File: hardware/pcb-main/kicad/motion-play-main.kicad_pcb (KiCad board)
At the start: 4 copper layers, 101.4 x 40 mm, 86 parts, among them IC1 SN74AHCT125PWR, J3 LED_Strip, J4 Conn_01x05, J5 Conn_01x05, J6 Conn_01x05, J7 TYPE-C-31-M-12, J8 JST_PH_2pin, Q2 PMOS, U1 AP2112K-3.3TRG1, U2 T-Display-S3, U4 TCA9548APWR, U5 BQ24195RGER, U6 TPS61088RHLR, U7 INA219AIDCNR

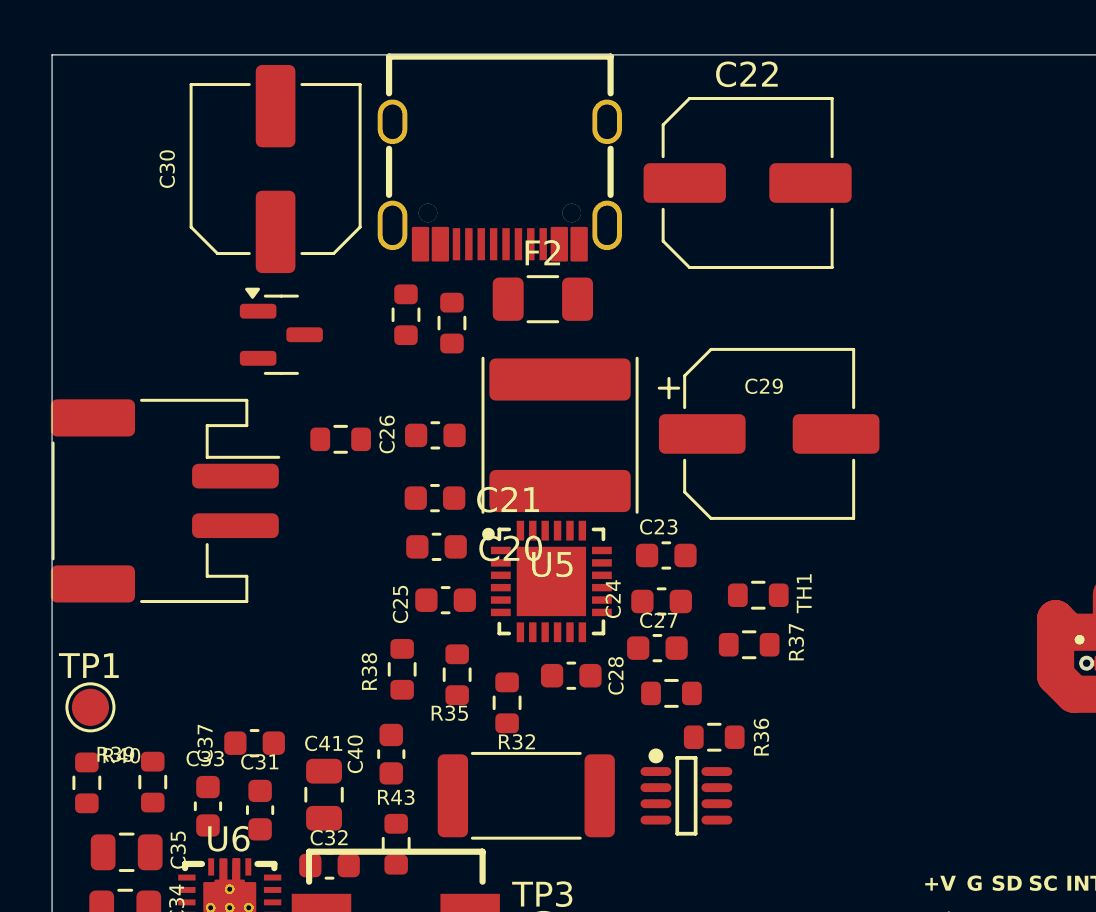
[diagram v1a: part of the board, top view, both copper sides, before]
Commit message: Phase 3 complete: shift L1 up 2mm, re-place C23 to 3mm from BTST, run DRC
L1 moved from y=116.35 to y=114.35, opening a 2.1mm gap between L1 and U5.
C23 BTST bridging cap improved from 4.5mm (relaxed) to 3.0mm (within Tier 1).
Relaxation count reduced from 4 to 2 (only L2 and C41 remain relaxed).

DRC: 84 violations total — 56 from J7/U6 footprint imports (pre-existing),
17 silkscreen overlaps (cosmetic), 9 dangling tracks (pre-existing),
2 R42 edge clearance (only placement-caused issue). 137 unconnected items
expected pre-routing. No component overlap violations.

Made-with: Cursor
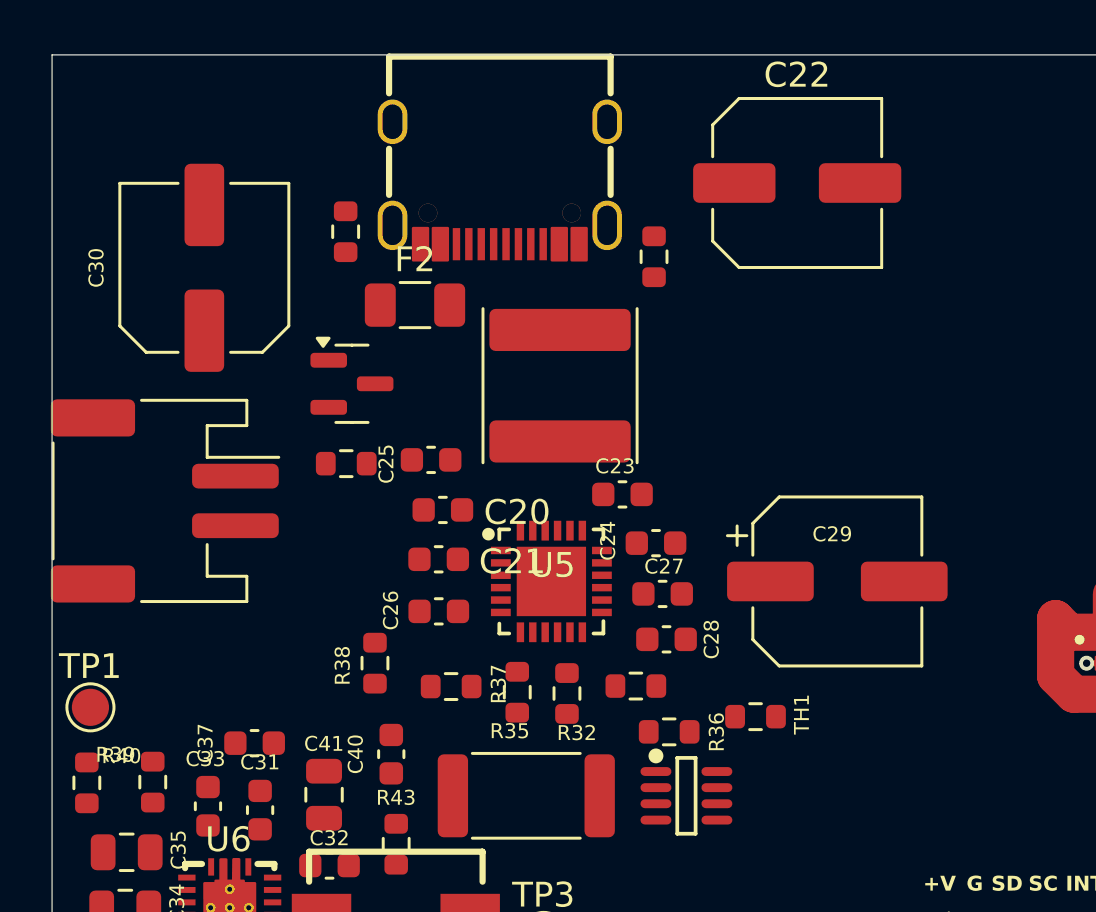
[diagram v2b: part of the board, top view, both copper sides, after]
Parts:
- moved R37 12.1 mm to (78.7, 126.5)
- moved R30 8.58 mm to (86.9, 109.1)
- moved C26 7.10 mm to (78.2, 123.5)
- moved C29 6.56 mm to (94.3, 122.2)
- moved C25 5.69 mm to (77.9, 117.3)
- moved F2 5.17 mm to (77.2, 111.1)
- moved C30 4.92 mm to (68.7, 109.6)
- moved TH1 4.90 mm to (91.0, 127.7)
- moved R31 4.14 mm to (74.4, 108.1)
- moved C28 4.11 mm to (87.4, 124.6)
- moved Q2 3.47 mm to (74.7, 114.3)
- moved C23 3.03 mm to (85.6, 118.7)
- moved R35 2.53 mm to (81.4, 126.7)
- moved C21 2.47 mm to (78.2, 121.4)
- moved R32 2.45 mm to (83.4, 126.8)
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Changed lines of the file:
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@@
 	(footprint "Capacitor_SMD:C_0603_1608Metric"
 		(layer "F.Cu")
-		(at 78.067 116.355 180)
+		(at 78.206 123.457 180)
 		(descr "Capacitor SMD 0603 (1608 Metric), square (rectangular) end terminal, IPC-7351 nominal, (Body size source: IPC-SM-782 page 76, https://www.pcb-3d.com/wordpress/wp-content/uploads/ipc-sm-782a_amendment_1_and_2.pdf), generated with kicad-footprint-generator")
 		(tags "capacitor")
@@
 	(footprint "Resistor_SMD:R_0603_1608Metric"
 		(layer "F.Cu")
-		(at 90.732 124.805)
+		(at 78.705 126.491)
 		(descr "Resistor SMD 0603 (1608 Metric), square (rectangular) end terminal, IPC-7351 nominal, (Body size source: IPC-SM-782 page 72, https://www.pcb-3d.com/wordpress/wp-content/uploads/ipc-sm-782a_amendment_1_and_2.pdf), generated with kicad-footprint-generator")
 		(tags "resistor")
@@
 	(footprint "Resistor_SMD:R_0603_1608Metric"
 		(layer "F.Cu")
-		(at 78.948 126.013 -90)
+		(at 81.373 126.72 -90)
 		(descr "Resistor SMD 0603 (1608 Metric), square (rectangular) end terminal, IPC-7351 nominal, (Body size source: IPC-SM-782 page 72, https://www.pcb-3d.com/wordpress/wp-content/uploads/ipc-sm-782a_amendment_1_and_2.pdf), generated with kicad-footprint-generator")
 		(tags "resistor")
@@
 	(footprint "Resistor_SMD:R_0603_1608Metric"
 		(layer "F.Cu")
-		(at 74.247 116.514)
+		(at 74.472 117.496)
 		(descr "Resistor SMD 0603 (1608 Metric), square (rectangular) end terminal, IPC-7351 nominal, (Body size source: IPC-SM-782 page 72, https://www.pcb-3d.com/wordpress/wp-content/uploads/ipc-sm-782a_amendment_1_and_2.pdf), generated with kicad-footprint-generator")
 		(tags "resistor")
@@
 	(footprint "Capacitor_SMD:C_0603_1608Metric"
 		(layer "F.Cu")
-		(at 87.029 124.94)
+		(at 87.239 122.753)
 		(descr "Capacitor SMD 0603 (1608 Metric), square (rectangular) end terminal, IPC-7351 nominal, (Body size source: IPC-SM-782 page 76, https://www.pcb-3d.com/wordpress/wp-content/uploads/ipc-sm-782a_amendment_1_and_2.pdf), generated with kicad-footprint-generator")
 		(tags "capacitor")
@@
 	(footprint "Capacitor_SMD:CP_Elec_6.3x7.7"
 		(layer "F.Cu")
-		(at 91.539 116.296)
+		(at 94.29 122.25)
 		(descr "SMD capacitor, aluminum electrolytic, Nichicon, 6.3x7.7mm")
 		(tags "capacitor electrolytic")
@@
 	(footprint "Package_TO_SOT_SMD:SOT-23"
 		(layer "F.Cu")
-		(at 71.854 112.294)
+		(at 74.702 114.273)
 		(descr "SOT, 3 Pin (JEDEC TO-236 Var AB https://www.jedec.org/document_search?search_api_views_fulltext=TO-236), generated with kicad-footprint-generator ipc_gullwing_generator.py")
 		(tags "SOT TO_SOT_SMD")
@@
 	(footprint "Resistor_SMD:R_0603_1608Metric"
 		(layer "F.Cu")
-		(at 91.1 122.806)
+		(at 90.989 127.706)
 		(descr "Resistor SMD 0603 (1608 Metric), square (rectangular) end terminal, IPC-7351 nominal, (Body size source: IPC-SM-782 page 72, https://www.pcb-3d.com/wordpress/wp-content/uploads/ipc-sm-782a_amendment_1_and_2.pdf), generated with kicad-footprint-generator")
 		(tags "resistor")
@@
 	(footprint "Capacitor_SMD:C_0603_1608Metric"
 		(layer "F.Cu")
-		(at 78.053 118.887)
+		(at 78.202 121.356)
 		(descr "Capacitor SMD 0603 (1608 Metric), square (rectangular) end terminal, IPC-7351 nominal, (Body size source: IPC-SM-782 page 76, https://www.pcb-3d.com/wordpress/wp-content/uploads/ipc-sm-782a_amendment_1_and_2.pdf), generated with kicad-footprint-generator")
 		(tags "capacitor")
@@
 	(footprint "Capacitor_SMD:C_0603_1608Metric"
 		(layer "F.Cu")
-		(at 83.554 126.054)
+		(at 87.397 124.586)
 		(descr "Capacitor SMD 0603 (1608 Metric), square (rectangular) end terminal, IPC-7351 nominal, (Body size source: IPC-SM-782 page 76, https://www.pcb-3d.com/wordpress/wp-content/uploads/ipc-sm-782a_amendment_1_and_2.pdf), generated with kicad-footprint-generator")
 		(tags "capacitor")
@@
 	(footprint "Capacitor_SMD:C_0603_1608Metric"
 		(layer "F.Cu")
-		(at 87.199 123.058 180)
+		(at 86.972 120.704 180)
 		(descr "Capacitor SMD 0603 (1608 Metric), square (rectangular) end terminal, IPC-7351 nominal, (Body size source: IPC-SM-782 page 76, https://www.pcb-3d.com/wordpress/wp-content/uploads/ipc-sm-782a_amendment_1_and_2.pdf), generated with kicad-footprint-generator")
 		(tags "capacitor")
@@
 	(footprint "Capacitor_SMD:C_0603_1608Metric"
 		(layer "F.Cu")
-		(at 78.116 120.854)
+		(at 78.371 119.364)
 		(descr "Capacitor SMD 0603 (1608 Metric), square (rectangular) end terminal, IPC-7351 nominal, (Body size source: IPC-SM-782 page 76, https://www.pcb-3d.com/wordpress/wp-content/uploads/ipc-sm-782a_amendment_1_and_2.pdf), generated with kicad-footprint-generator")
 		(tags "capacitor")
@@
 	(footprint "Resistor_SMD:R_0603_1608Metric"
 		(layer "F.Cu")
-		(at 87.596 126.768)
+		(at 86.159 126.471)
 		(descr "Resistor SMD 0603 (1608 Metric), square (rectangular) end terminal, IPC-7351 nominal, (Body size source: IPC-SM-782 page 72, https://www.pcb-3d.com/wordpress/wp-content/uploads/ipc-sm-782a_amendment_1_and_2.pdf), generated with kicad-footprint-generator")
 		(tags "resistor")
@@
 	(footprint "Capacitor_SMD:C_0603_1608Metric"
 		(layer "F.Cu")
-		(at 78.482 123.006 180)
+		(at 77.896 117.344 180)
 		(descr "Capacitor SMD 0603 (1608 Metric), square (rectangular) end terminal, IPC-7351 nominal, (Body size source: IPC-SM-782 page 76, https://www.pcb-3d.com/wordpress/wp-content/uploads/ipc-sm-782a_amendment_1_and_2.pdf), generated with kicad-footprint-generator")
 		(tags "capacitor")
@@
 	(footprint "Fuse:Fuse_1206_3216Metric"
 		(layer "F.Cu")
-		(at 82.407 110.859)
+		(at 77.246 111.097)
 		(descr "Fuse SMD 1206 (3216 Metric), square (rectangular) end terminal, IPC-7351 nominal, (Body size source: http://www.tortai-tech.com/upload/download/2011102023233369053.pdf), generated with kicad-footprint-generator")
 		(tags "fuse")
@@
 	(footprint "Resistor_SMD:R_0603_1608Metric"
 		(layer "F.Cu")
-		(at 89.323 128.536)
+		(at 87.504 128.32)
 		(descr "Resistor SMD 0603 (1608 Metric), square (rectangular) end terminal, IPC-7351 nominal, (Body size source: IPC-SM-782 page 72, https://www.pcb-3d.com/wordpress/wp-content/uploads/ipc-sm-782a_amendment_1_and_2.pdf), generated with kicad-footprint-generator")
 		(tags "resistor")
@@
 	(footprint "Capacitor_SMD:C_0603_1608Metric"
 		(layer "F.Cu")
-		(at 87.387 121.201 180)
+		(at 85.619 118.737 180)
 		(descr "Capacitor SMD 0603 (1608 Metric), square (rectangular) end terminal, IPC-7351 nominal, (Body size source: IPC-SM-782 page 76, https://www.pcb-3d.com/wordpress/wp-content/uploads/ipc-sm-782a_amendment_1_and_2.pdf), generated with kicad-footprint-generator")
 		(tags "capacitor")
@@
 	(footprint "Resistor_SMD:R_0603_1608Metric"
 		(layer "F.Cu")
-		(at 78.738 111.822 -90)
+		(at 86.894 109.146 -90)
 		(descr "Resistor SMD 0603 (1608 Metric), square (rectangular) end terminal, IPC-7351 nominal, (Body size source: IPC-SM-782 page 72, https://www.pcb-3d.com/wordpress/wp-content/uploads/ipc-sm-782a_amendment_1_and_2.pdf), generated with kicad-footprint-generator")
 		(tags "resistor")
@@
 	(footprint "Resistor_SMD:R_0603_1608Metric"
 		(layer "F.Cu")
-		(at 80.963 127.147 -90)
+		(at 83.379 126.771 -90)
 		(descr "Resistor SMD 0603 (1608 Metric), square (rectangular) end terminal, IPC-7351 nominal, (Body size source: IPC-SM-782 page 72, https://www.pcb-3d.com/wordpress/wp-content/uploads/ipc-sm-782a_amendment_1_and_2.pdf), generated with kicad-footprint-generator")
 		(tags "resistor")
@@
 	(footprint "Capacitor_SMD:C_Elec_6.3x5.4"
 		(layer "F.Cu")
-		(at 90.67 106.17)
+		(at 92.67 106.17)
 		(descr "SMD capacitor, aluminum electrolytic nonpolar, 6.3x5.4mm")
 		(tags "capacitor electrolytic nonpolar")
@@
 	(footprint "Resistor_SMD:R_0603_1608Metric"
 		(layer "F.Cu")
-		(at 76.729 125.797 -90)
+		(at 75.631 125.547 -90)
 		(descr "Resistor SMD 0603 (1608 Metric), square (rectangular) end terminal, IPC-7351 nominal, (Body size source: IPC-SM-782 page 72, https://www.pcb-3d.com/wordpress/wp-content/uploads/ipc-sm-782a_amendment_1_and_2.pdf), generated with kicad-footprint-generator")
 		(tags "resistor")
@@
 	(footprint "Inductor_SMD:L_Changjiang_FNR6028S"
 		(layer "F.Cu")
-		(at 83.1 116.35 90)
+		(at 83.1 114.35 90)
 		(descr "Inductor, Changjiang, FNR6028S, 6.0x6.0x2.8mm, (https://datasheet.lcsc.com/lcsc/1806131217_cjiang-Changjiang-Microelectronics-Tech-FNR5040S3R3NT_C167960.pdf), generated with kicad-footprint-generator gen_inductor.py")
 		(tags "wirewound power shielded")
@@
 	(footprint "Resistor_SMD:R_0603_1608Metric"
 		(layer "F.Cu")
-		(at 76.883 111.487 -90)
+		(at 74.448 108.136 -90)
 		(descr "Resistor SMD 0603 (1608 Metric), square (rectangular) end terminal, IPC-7351 nominal, (Body size source: IPC-SM-782 page 72, https://www.pcb-3d.com/wordpress/wp-content/uploads/ipc-sm-782a_amendment_1_and_2.pdf), generated with kicad-footprint-generator")
 		(tags "resistor")
@@
 	(footprint "Capacitor_SMD:C_Elec_6.3x5.4"
 		(layer "F.Cu")
-		(at 71.621 105.606 90)
+		(at 68.745 109.593 90)
 		(descr "SMD capacitor, aluminum electrolytic nonpolar, 6.3x5.4mm")
 		(tags "capacitor electrolytic nonpolar")

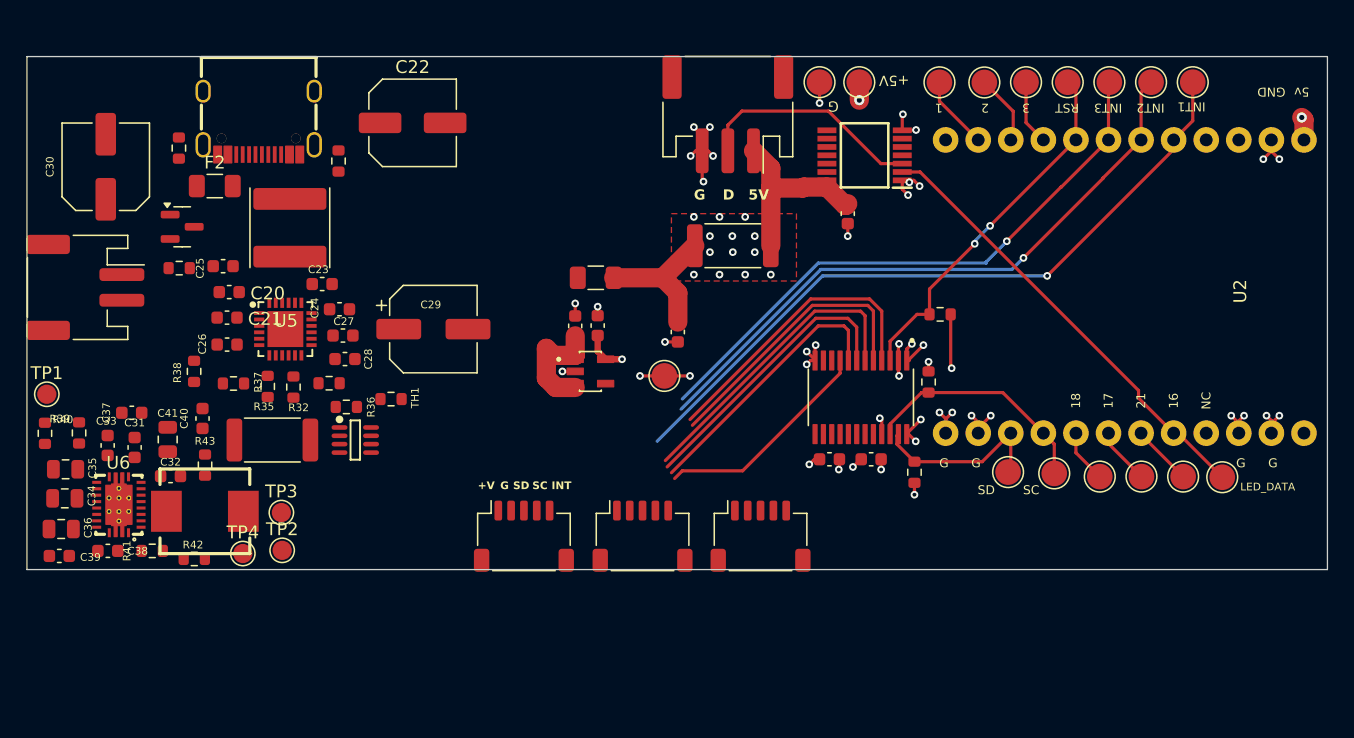
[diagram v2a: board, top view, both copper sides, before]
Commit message: Fix L2 bbox, re-place power components, complete full board routing
- Fix extract.py inductor bbox heuristic: parse L{X}-W{Y} from footprint
  name when pad-based bbox height < width/2 (L2: 8.4×3.2 → 8.4×6.6mm)
- Add L2 to placement anchors, re-run placement pushing C32/R41/R42/R43/TP4
  out of L2's physical footprint
- Fix J7 USB-C schematic pin-to-footprint mapping (A4→A4B9, etc.)
- Complete all trace routing: power switching loops (BOOST_SW pour, BQ_SW),
  VSYS/VBAT/Protected_VBUS power paths, INA219 Kelvin sense, +5V distribution
  via In2.Cu zone, I2C bus, all U5/U6 support passives
- Board setup: net classes, design rules, zone fills
- DRC: 0 unconnected pads, remaining violations are easyeda2kicad footprint
  artifacts (U6 thermal vias, J7 pad spacing) and expected tight QFN escapes

Made-with: Cursor
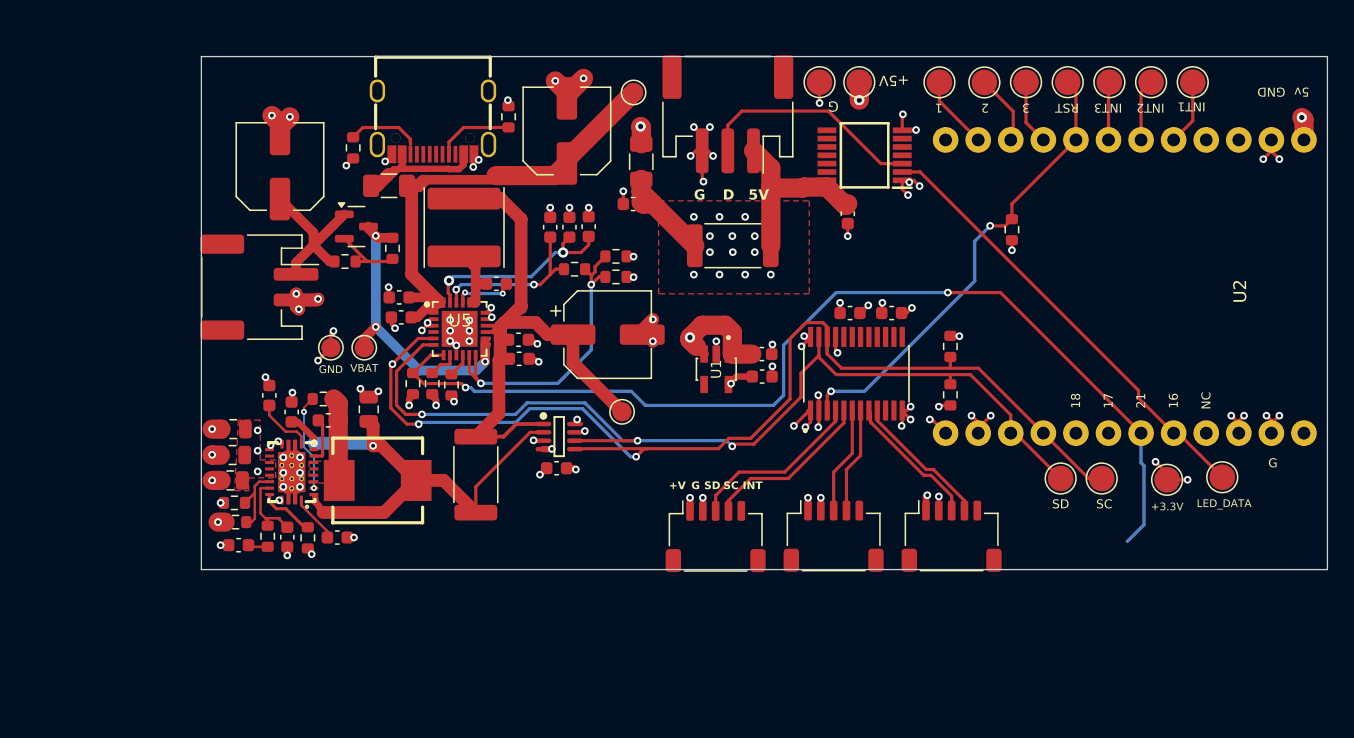
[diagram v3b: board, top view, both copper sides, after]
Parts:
- removed TPIO17, TPIO18, TPIO21: TestPoint, TestPoint:TestPoint_Pad_D2.0mm
- moved TP1 44.9 mm to (109.0, 128.7)
- moved TP3 42.7 mm to (109.9, 103.8)
- moved TP_3V1 40.0 mm to (151.5, 134.0)
- moved J6 33.3 mm to (134.7, 138.4)
- moved R37 31.0 mm to (108.5, 118.2)
- moved C25 28.7 mm to (106.4, 114.3), turned to 90 degrees
- moved C26 28.2 mm to (104.9, 114.3), turned to 90 degrees
- moved C40 27.9 mm to (103.9, 133.1), turned to 180 degrees
- moved R36 20.8 mm to (105.3, 117.6)
- moved TH1 20.8 mm to (108.5, 116.6)
- moved C33 19.3 mm to (86.8, 138.5), turned to 0 degrees
- moved C39 17.8 mm to (82.9, 138.5), turned to -90 degrees
- moved R41 17.8 mm to (85.7, 127.7)
- moved C24 17.6 mm to (103.4, 114.3), turned to 90 degrees
- moved TP4 17.5 mm to (86.3, 123.7)
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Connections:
- J7 pad A1B12: (no net) -> GND
- J7 pad A4B9: (no net) -> /Power Management/VBUS_RAW
- J7 pad B1A12: (no net) -> GND
- J7 pad B4A9: (no net) -> /Power Management/VBUS_RAW
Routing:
- net /Power Management/CHRG_INT: track 4.75 -> 80.4 mm, vias 0 -> 2
- net /I2C_SCL: track 19.4 -> 88.1 mm, vias 0 -> 3
- net /I2C_SDA: track 14.8 -> 76.8 mm, vias 0 -> 3
- net /INT1: track 55.6 -> 5.86 mm, vias 1 -> 0
- net /Power Management/VSYS: track 0.00 -> 47.5 mm
- net /INT2: track 49.6 -> 5.04 mm, vias 1 -> 0
- net GND: track 50.1 -> 94.0 mm, vias 49 -> 113
- net /INT3: track 46.6 -> 4.98 mm, vias 1 -> 0
- net /Power Management/VSYS_SENSE: track 0.00 -> 39.7 mm, vias 0 -> 2
- net /Power Management/Protected_VBUS: track 0.00 -> 35.9 mm
- net /Power Management/BQ_TS: track 0.00 -> 24.4 mm, vias 0 -> 2
- net /Power Management/VBAT: track 0.00 -> 23.2 mm, vias 0 -> 3
- net /Power Management/BQ_PMID: track 0.00 -> 15.9 mm, vias 0 -> 2
- net /TCA9548A_Subsystem/CH1_SDA: track 24.0 -> 8.40 mm
- net /Power Management/VBUS_RAW: track 0.00 -> 14.3 mm
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- added copper zone on F.Cu, net +5V
- added copper zone on F.Cu, net /Power Management/BOOST_SW
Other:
- board size 101.4 x 40 mm -> 87.8 x 40 mm
